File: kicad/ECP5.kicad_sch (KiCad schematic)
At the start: 69 parts, among them J1 HDMI_A, J2 031-71052, Q1 MMST2222A, SW1 Reset, T1 DA101JC, U1 TPS22948, U2 IS25LP128F, U3 DSLVDS1047, U4 LFE5U-12F-6TG144C, U5 74HC04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

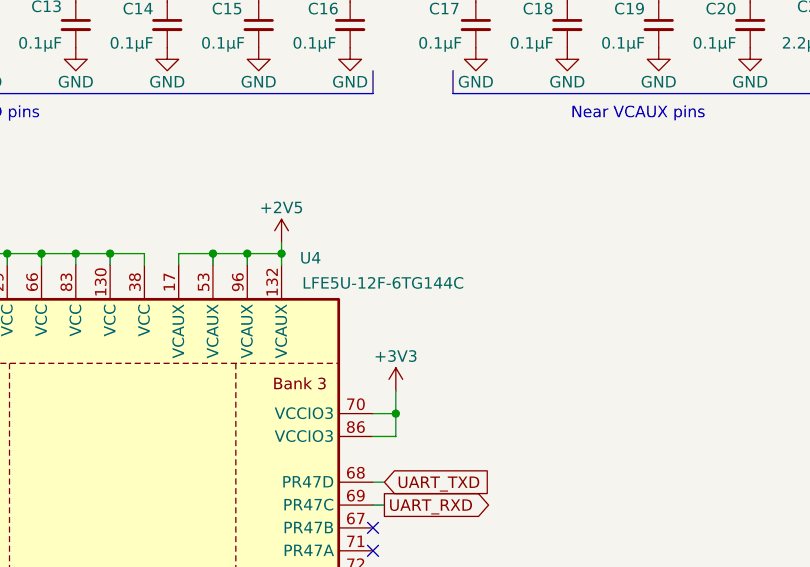
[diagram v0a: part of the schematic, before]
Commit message: Upgraded to ECP5-25K
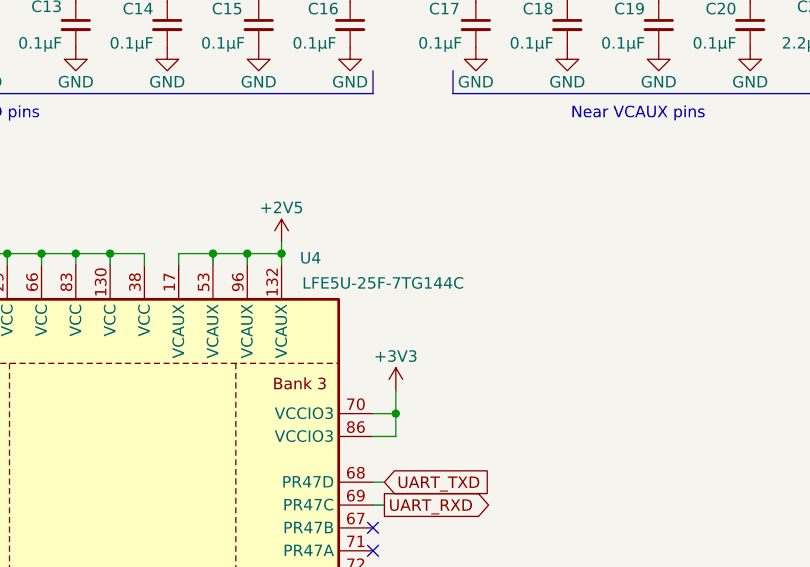
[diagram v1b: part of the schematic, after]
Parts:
- U4: value LFE5U-12F-6TG144C -> LFE5U-25F-7TG144C; MPN LFE5U-12F-6TG144C -> LFE5U-25F-7TG144C
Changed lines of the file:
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@@
 			)
 		)
-		(property "Value" "LFE5U-12F-6TG144C"
+		(property "Value" "LFE5U-25F-7TG144C"
 			(at 181.356 51.562 0)
 			(effects
@@
 			)
 		)
-		(property "Description" "IC FPGA ECP5 12K LUT 144TQFP"
+		(property "Description" "IC FPGA ECP5 24K LUT 144TQFP"
 			(at 162.56 209.55 0)
 			(effects
@@
 			)
 		)
-		(property "MPN" "LFE5U-12F-6TG144C"
+		(property "MPN" "LFE5U-25F-7TG144C"
 			(at 162.56 161.29 0)
 			(effects

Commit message: 5.1K USB resistors
Replaces 22K resistors to VBUS with 5.1K resistors to GND.
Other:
- note added: "B"
- note added: "ECP5 Ultra Plus Audio TX"
- note removed: "A"
- note removed: "ECP5 Ultra Plus Audio Tx"
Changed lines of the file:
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@@
 		)
 	)
-	(text "ECP5 Ultra Plus Audio Tx"
+	(text "ECP5 Ultra Plus Audio TX"
 		(exclude_from_sim no)
-		(at 327.914 258.826 0)
+		(at 303.276 258.826 0)
 		(effects
 			(font
@@
 				(bold yes)
 			)
+			(justify left)
 		)
 	)
@@
 		)
 	)
-	(text "A"
+	(text "B"
 		(exclude_from_sim no)
 		(at 392.684 280.416 0)
